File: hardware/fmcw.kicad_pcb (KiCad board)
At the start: 4 copper layers, 147.8 x 68.6 mm, 425 parts, among them CON1 BARREL_JACK, J1 SD_Card, J2 USB_B_Micro, J3 SMA, J4 SMA, J5 SMA, P1 CONN_02X04, P2 CONN_02X04, Q1 DNP(RE1C002UN), Q2 RE1C002UN, SW1 SW_PUSH, U1 LP5907MFX-3.3, U10 LP5907MFX-3.0, U11 LTC2292, U12 ADF4158, U13 TLV172DCK, U14 PAT1220-3dB, U15 HMC431LP4, U16 PD4859J5050S2HF, U17 PAT1220-5dB, U18 SE5004L, U19 DC4759J5020AHF, U2 LP5907MFX-1.8, U20 PAT1220-6dB, U22 TRF37A73, U23 SKY65404, U24 TRF37A73, U25 SKY65404, U26 TPS5420D, U27 TPS5420D, U28 TPS560200, U29 LP2985A-10DBVR, U3 KT2520K-T, U30 TPS7A7001DDA, U31 TPS7A91, U32 TPS7A91, U33 LP5907MFX-3.0, U34 TPS7A91, U35 5400BL15B050E, U36 5400BL15B050E, U37 5400BL15B050E, U38 ADL5802, U39 ADA4940-2, U4 NC7SVU04P5X, U5 NB3N551, U6 XC7A15T-FTG256, U7 W25Q32JV, U8 93LCxxB, U9 FT2232H, Y1 12MHz

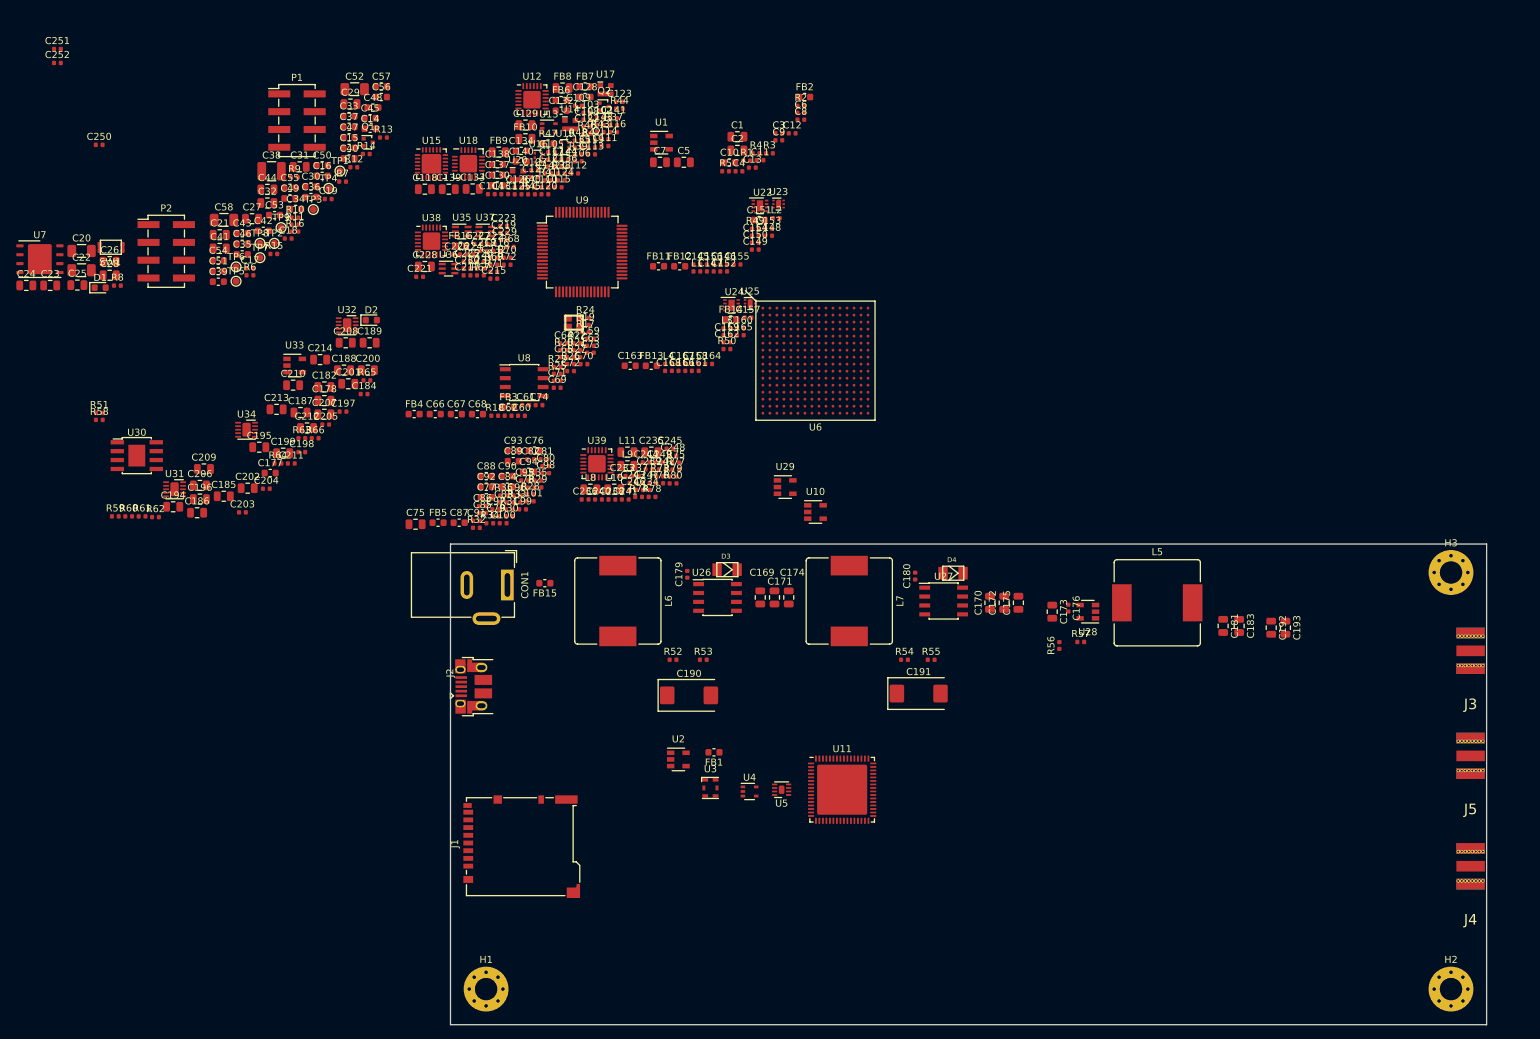
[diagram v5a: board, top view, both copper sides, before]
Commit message: Placed most major components.
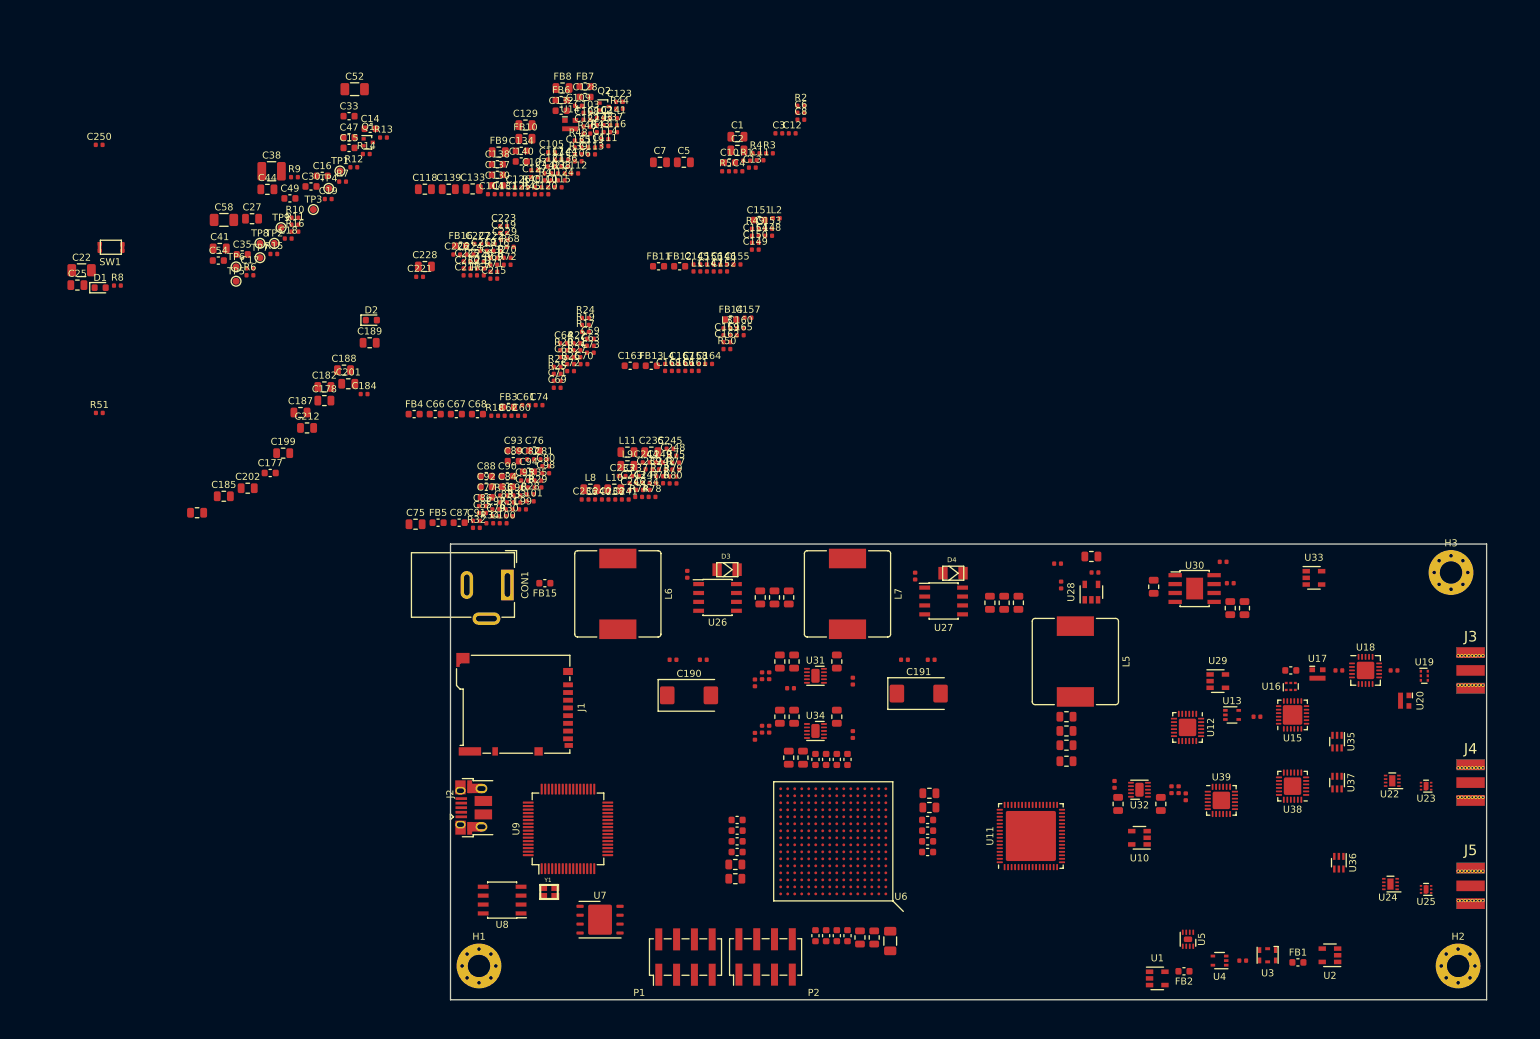
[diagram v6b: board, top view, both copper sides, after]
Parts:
- moved C252 209.5 mm to (221.0, 105.7), turned to 180 degrees
- moved C251 203.2 mm to (213.1, 105.7), turned to 180 degrees
- moved R59 159.4 mm to (197.6, 93.2), turned to 180 degrees
- moved R60 156.3 mm to (196.6, 90.2), turned to 180 degrees
- moved U36 152.7 mm to (213.1, 133.1), turned to 270 degrees
- moved U30 152.1 mm to (192.5, 94.0)
- moved C20 151.7 mm to (149.1, 144.3), turned to 270 degrees
- moved U33 148.5 mm to (209.6, 92.5)
- moved m 148.3 mm to (144.8, 143.8), turned to 270 degrees
- moved C206 148.0 mm to (197.6, 96.8), turned to 270 degrees
- moved U20 147.1 mm to (222.5, 110.0), turned to 270 degrees
- moved U18 147.0 mm to (216.9, 105.7)
- moved U15 145.9 mm to (206.5, 112.0), turned to 90 degrees
- moved U38 145.4 mm to (206.5, 122.2), turned to 180 degrees
- moved U37 144.7 mm to (212.9, 121.7), turned to 270 degrees
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- renumbered C23 to m
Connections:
- R4 pad 1: /FPGA_REF -> /ADF_REF
- R5 pad 1: /ADF_REF -> /FPGA_REF
- U17 pad 1: Net-(C251-Pad2) -> Net-(R47-Pad1)
- U17 pad 2: Net-(R47-Pad1) -> Net-(C251-Pad2)
- U20 pad 1: /LO -> Net-(U19-Pad2)
- U20 pad 2: Net-(U19-Pad2) -> /LO
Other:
- board size 147.8 x 68.6 mm -> 147.8 x 65 mm

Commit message: Completed clock placement and routing.
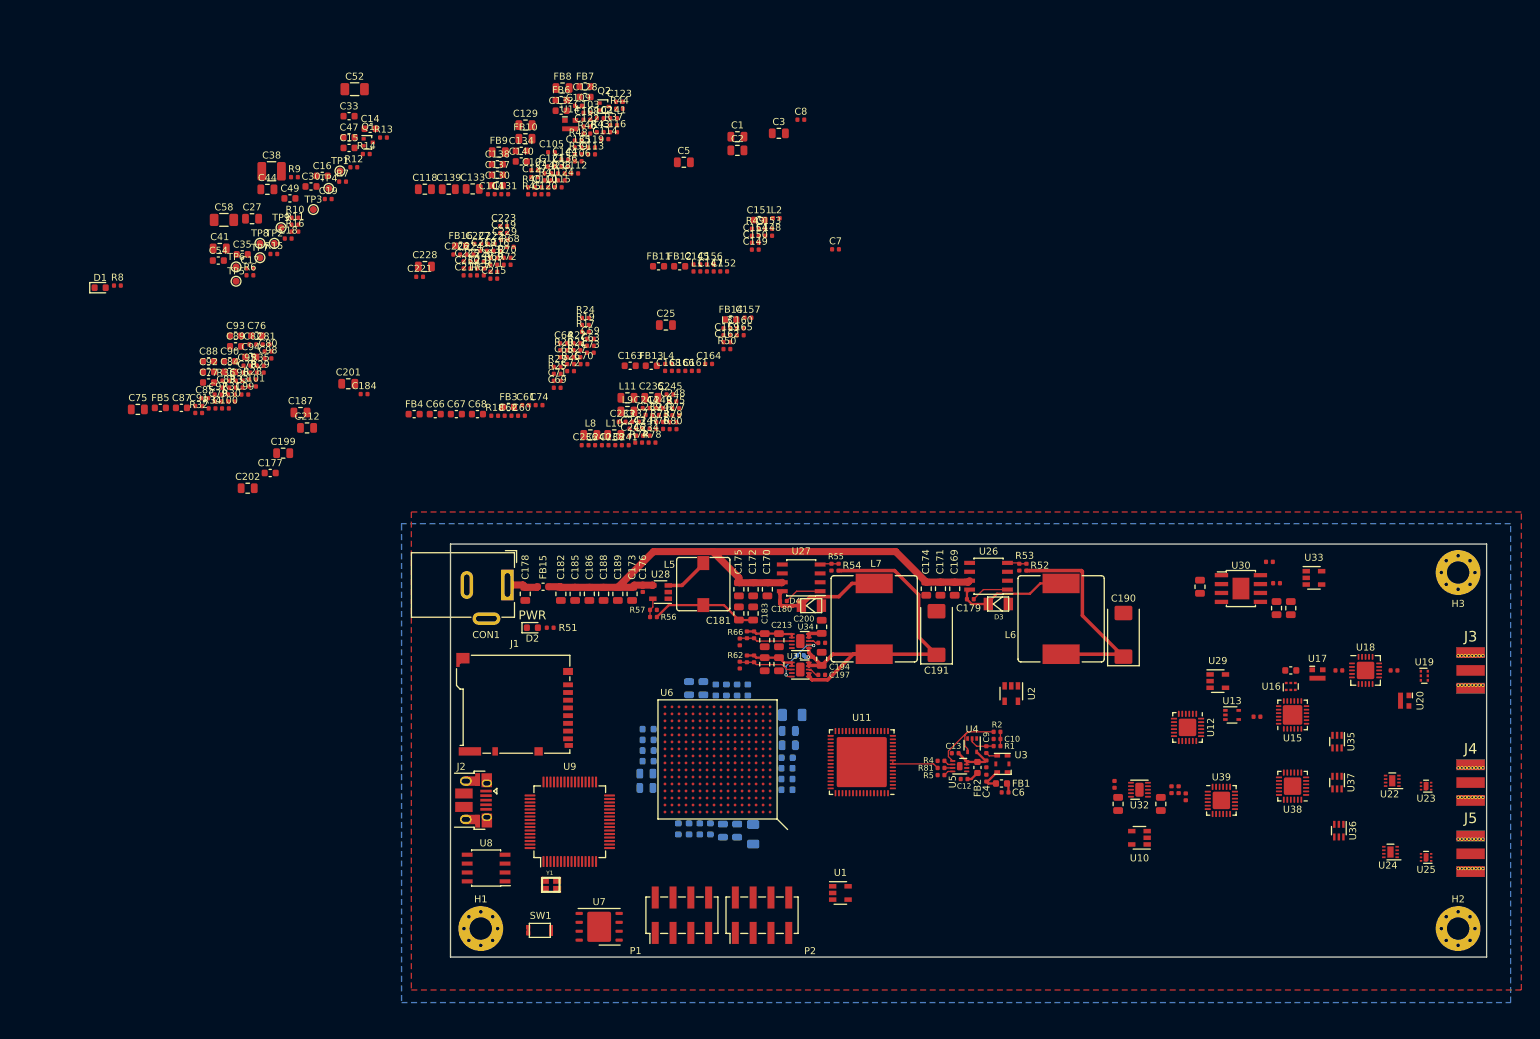
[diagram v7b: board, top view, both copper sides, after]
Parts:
- removed C111, C117, C125, C126, C143, C146, C155, C158, C167, C250, C86: 100n, Capacitor_SMD:C_0402_1005Metric
- removed C192, C193: 10u, Capacitor_SMD:C_0805_2012Metric
- removed R3: 1k, Resistor_SMD:R_0402_1005Metric
- added R81: 33, Resistor_SMD:R_0402_1005Metric, F.Cu at (156.3, 119.6)
- C1: value DNP -> 10u
- C10: value 4.7u -> 10n; footprint Capacitor_SMD:C_0603_1608Metric -> Capacitor_SMD:C_0402_1005Metric
- C20, C21, C22, C24, C26, C28, C29, C31, C32, C34, C36, C37, C39, C40, C42, C43, C45, C46, C48, C50, C51, C53, C55, C56, C57, R58: moved to B.Cu
- C23: renamed from m; moved to B.Cu
- C3: value 100n -> 10u; footprint Capacitor_SMD:C_0402_1005Metric -> Capacitor_SMD:C_0805_2012Metric
- C7: value DNP -> 100n; footprint Capacitor_SMD:C_0805_2012Metric -> Capacitor_SMD:C_0402_1005Metric
- C9: value 100n -> 10n
- L5: value 33u -> 10u; footprint Inductor_SMD:L_Bourns_SRR1210A -> Inductor_SMD:L_Wuerth_WE-PD-Typ-7345
- R1: value 49.9 -> 470k
- R2: value 1k -> 470k
- moved C22 119.6 mm to (135.1, 112.0)
- moved SW1 116.8 mm to (100.7, 142.7), turned to 180 degrees
- moved C6 101.3 mm to (165.5, 123.1), turned to 180 degrees
- moved C12 95.3 mm to (159.6, 121.2), turned to 180 degrees
- moved R2 93.6 mm to (164.3, 114.4)
- moved C4 93.5 mm to (162.8, 121.0), turned to 270 degrees
- moved C11 92.0 mm to (162.8, 119.0), turned to 90 degrees
- moved R5 91.5 mm to (156.3, 120.6)
- moved R1 90.8 mm to (164.3, 116.5), turned to 180 degrees
- moved C10 90.7 mm to (164.3, 115.4)
- moved R4 90.6 mm to (156.3, 118.6)
- moved C13 88.4 mm to (158.4, 117.5)
- moved C25 84.2 mm to (117.1, 56.4)
- moved R51 71.3 mm to (100.6, 99.6), turned to 180 degrees
- moved C173 65.7 mm to (112.3, 94.7), turned to 270 degrees
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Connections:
- C10 pad 1: Net-(C10-Pad1) -> GND
- C10 pad 2: GND -> Net-(C10-Pad2)
- C11 pad 2: Net-(C10-Pad1) -> Net-(C11-Pad2)
- C115 pad 1: /10V -> GND
- C115 pad 2: GND -> /10V
- C118 pad 1: Net-(C117-Pad1) -> GND
- C118 pad 2: GND -> Net-(C118-Pad2)
- C119 pad 1: Net-(C117-Pad1) -> GND
- C119 pad 2: GND -> Net-(C118-Pad2)
- C13 pad 1: Net-(C10-Pad1) -> GND
- C13 pad 2: GND -> Net-(C11-Pad2)
- C3 pad 1: /3V6 -> /1V8_OSC
- C4 pad 1: /1V8_OSC -> GND
- C4 pad 2: GND -> Net-(C4-Pad2)
- C6 pad 1: Net-(C6-Pad1) -> /1V8_OSC
- C65 pad 1: /3V3D -> GND
- C65 pad 2: GND -> /3V3D
- C7 pad 1: /3V3_INV -> /3V3D
- C8 pad 1: /1V8_OSC -> /3V3D
- FB1 pad 1: /1V8_OSC -> Net-(C4-Pad2)
- FB1 pad 2: Net-(C6-Pad1) -> /1V8_OSC
- FB2 pad 1: Net-(C10-Pad1) -> Net-(C11-Pad2)
- FB7 pad 1: Net-(C117-Pad1) -> Net-(C118-Pad2)
- R1 pad 1: Net-(C9-Pad2) -> Net-(C10-Pad2)
- R1 pad 2: GND -> Net-(C9-Pad1)
- R2 pad 1: Net-(C10-Pad1) -> Net-(R2-Pad1)
- R2 pad 2: Net-(C9-Pad1) -> Net-(C10-Pad2)
- U15 pad 20: Net-(C117-Pad1) -> Net-(C118-Pad2)
- U2 pad 5: Net-(C6-Pad1) -> /1V8_OSC
- U3 pad 6: /1V8_OSC -> Net-(C4-Pad2)
- U31 pad 7: /power/5V6 -> /3V6
- U4 pad 4: Net-(U4-Pad4) -> Net-(R2-Pad1)
- U4 pad 5: Net-(C10-Pad1) -> Net-(C11-Pad2)
- U5 pad 1: Net-(U4-Pad4) -> Net-(R2-Pad1)
- U5 pad 3: /ADC_REF -> Net-(R81-Pad2)
- U5 pad 7: Net-(C10-Pad1) -> Net-(C11-Pad2)
- U5 pad 8: Net-(C10-Pad1) -> Net-(C11-Pad2)
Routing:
- net /power/12V: track 0.00 -> 81.4 mm
- net /3V6: track 0.00 -> 60.5 mm, vias 0 -> 1
- net /power/5V6: track 0.00 -> 31.7 mm
- net Net-(C180-Pad1): track 0.00 -> 16.8 mm
- net Net-(C179-Pad1): track 0.00 -> 16.6 mm
- net /1V0: track 0.00 -> 15.3 mm
- net Net-(R2-Pad1): track 0.00 -> 12.5 mm
- net Net-(R58-Pad2): track 0.00 -> 8.07 mm, vias 0 -> 2
- net Net-(C204-Pad2): track 0.00 -> 7.89 mm
- net Net-(C211-Pad2): track 0.00 -> 7.61 mm
- net /1V8: track 0.00 -> 7.33 mm
- net /ADC_REF: track 0.00 -> 7.13 mm
- net /3V3D: track 0.00 -> 7.06 mm
- net Net-(C11-Pad2): track 0.00 -> 6.95 mm
- net Net-(L5-Pad1): track 0.00 -> 6.41 mm
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- added copper zone on B.Cu, net GND
- added copper zone on F.Cu, net GND
- added copper zone on In1.Cu, net GND
- added copper zone on In2.Cu, net GND
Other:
- board size 147.8 x 65 mm -> 147.8 x 58.9 mm
- net class 1.5A added: clearance 0.127, trace_width 0.508, via_dia 0.4572, via_drill 0.254
- net class 3A added: clearance 0.127, trace_width 1.016, via_dia 0.4572, via_drill 0.254
- net class Default: trace_width 0.1524 -> 0.127
- net class Power added: clearance 0.127, trace_width 0.3302, via_dia 0.4572, via_drill 0.254
- net class RF_50 added: clearance 0.127, trace_width 0.304292, via_dia 0.4572, via_drill 0.254
- rule trace_min: 0.1524 -> 0.127
- board text added: "PWR"

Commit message: Place/route for ft2232h.
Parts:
- moved R9 134.6 mm to (152.9, 136.4), turned to 270 degrees
- moved C8 109.8 mm to (97.8, 129.9), turned to 270 degrees
- moved C87 108.1 mm to (142.7, 120.1)
- moved C88 107.3 mm to (142.7, 118.6)
- moved C7 105.5 mm to (97.8, 141.7), turned to 90 degrees
- moved C93 104.7 mm to (140.5, 119.4), turned to 90 degrees
- moved C90 103.8 mm to (142.7, 116.8)
- moved C92 103.7 mm to (134.0, 126.4)
- moved C89 103.5 mm to (142.7, 115.3)
- moved R34 101.1 mm to (136.4, 124.5), turned to 270 degrees
- moved R32 101.1 mm to (134.5, 125.1)
- moved C96 99.8 mm to (139.2, 119.8), turned to 90 degrees
- moved C98 99.5 mm to (137.9, 123.4)
- moved C94 99.3 mm to (140.5, 116.1), turned to 270 degrees
- moved C97 99.2 mm to (139.2, 115.7), turned to 270 degrees
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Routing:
- net /fpga/TXE#: track 0.00 -> 45.7 mm
- net /fpga/RD#: track 0.00 -> 41.9 mm
- net /fpga/SIWUA: track 0.00 -> 38.7 mm, vias 0 -> 2
- net /fpga/WR: track 0.00 -> 38.6 mm
- net /fpga/EXT2_3: track 0.00 -> 38.1 mm
- net /fpga/EXT2_2: track 0.00 -> 36.5 mm
- net /fpga/OE#: track 0.00 -> 36.2 mm, vias 0 -> 2
- net /fpga/CLKOUT: track 0.00 -> 35.0 mm
- net /fpga/EXT1_3: track 0.00 -> 34.9 mm
- net /fpga/TDO: track 0.00 -> 34.6 mm, vias 0 -> 2
- net /fpga/EXT2_1: track 0.00 -> 34.5 mm
- net /fpga/FT_D5: track 0.00 -> 34.5 mm
- net /fpga/EXT1_2: track 0.00 -> 34.0 mm
- net /fpga/FT_D4: track 0.00 -> 34.0 mm
- net /fpga/FT_D7: track 0.00 -> 33.1 mm
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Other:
- rule pad_to_mask_clearance: 0.0508 -> 0.0381
